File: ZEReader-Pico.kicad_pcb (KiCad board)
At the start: 2 copper layers, 110 x 110 mm, 85 parts, among them J1 Micro_SD_Card_Det2, J2 UART, J3 SWD, J4 USB4105-GF-A, J6 Conn_01x02_Socket, J7 FFC2B28-24-G, Q1 Si1308EDL, Q2 DMG2305UX-7, SW1 SW_Push, SW2 SW_Push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

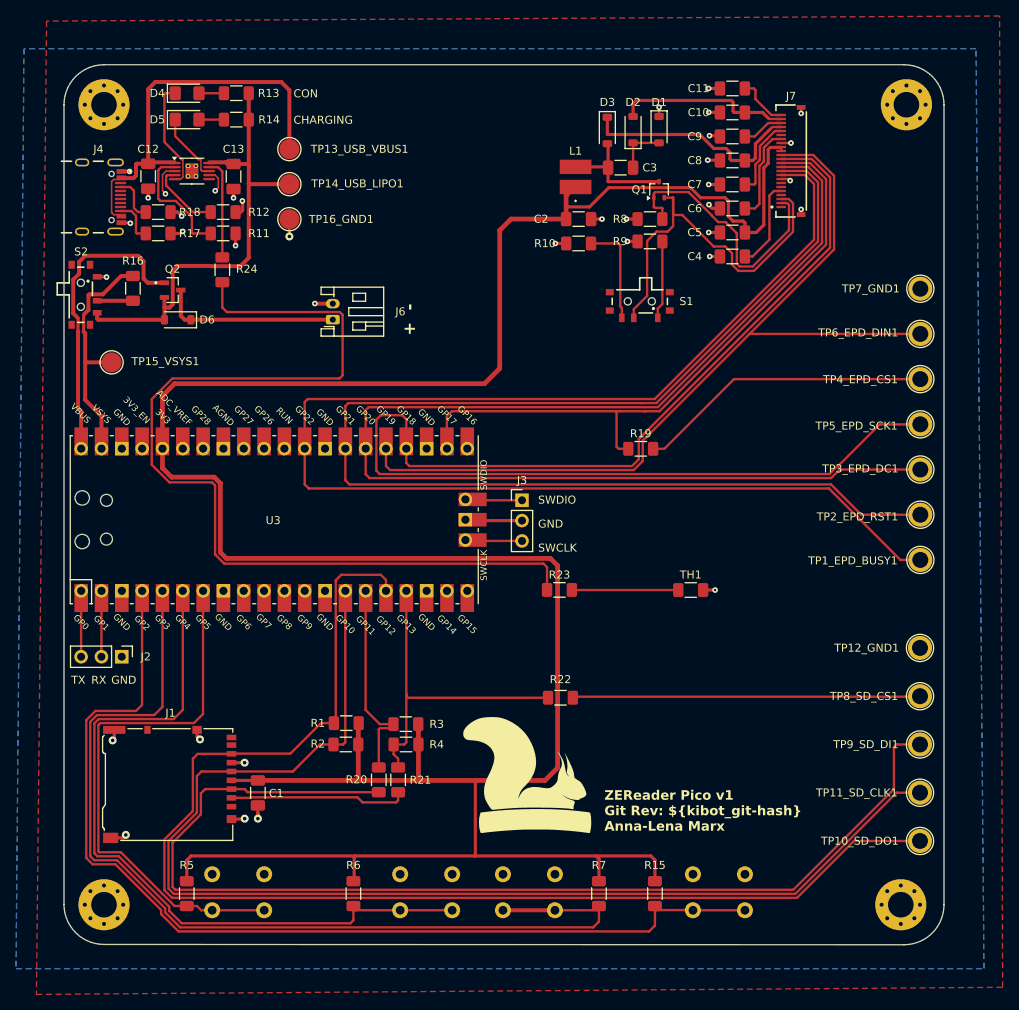
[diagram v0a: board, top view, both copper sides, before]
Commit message: Rerouted two parts
Signed-off-by: Anna-Lena Marx <anna-lena.marx@web.de>
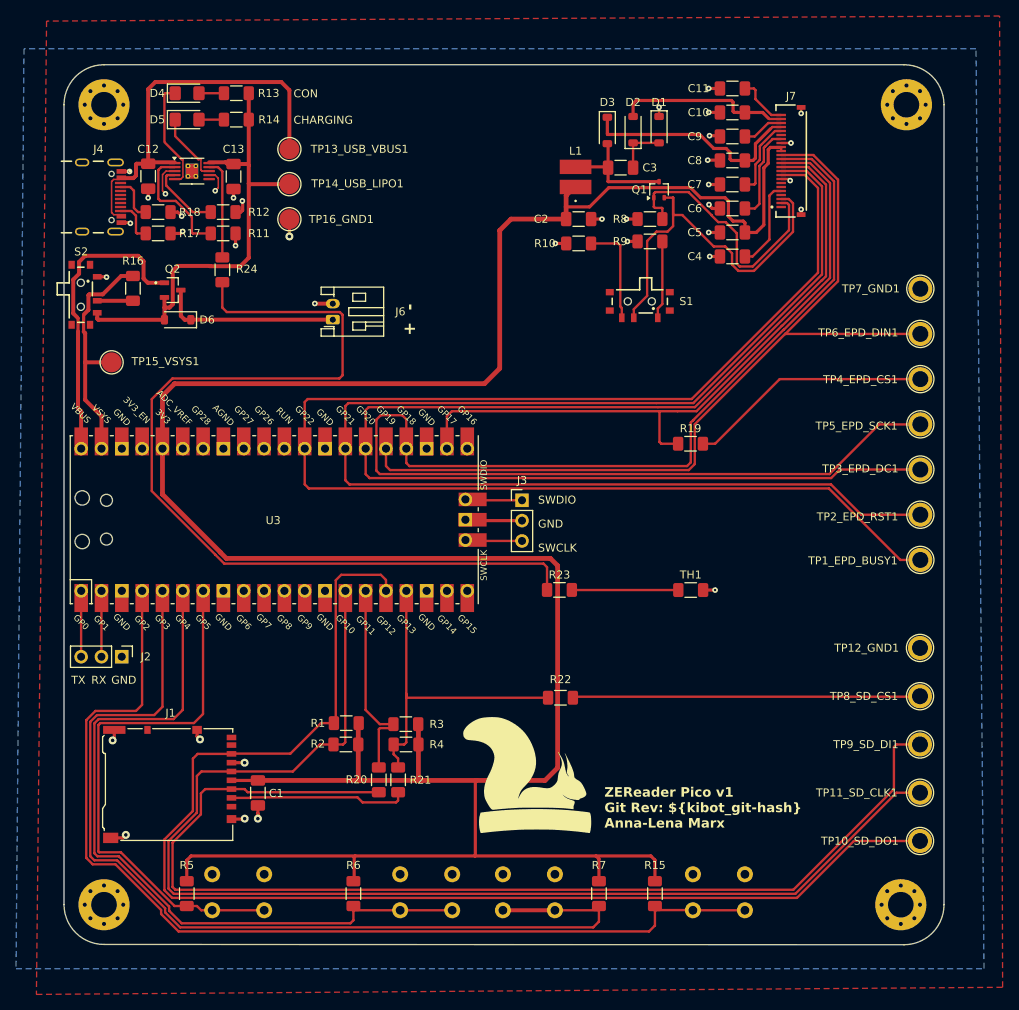
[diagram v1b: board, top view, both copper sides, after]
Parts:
- removed the G*** at (152.0, 131.3)
- removed REF**: KiCad-Logo2_6mm_SilkScreen, Symbol:KiCad-Logo2_6mm_SilkScreen
- added G***: LOGO, prj-footprints:Aisler, B.Cu at (151.6, 132.5)
- moved R19 6.26 mm to (178.4, 87.4)
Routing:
- net Net-(R19-Pad2): track 37.0 -> 30.5 mm
- net EPD_SCK: track 168.5 -> 173.0 mm
- net EPD_CS: track 81.2 -> 84.4 mm
- net EPD_DC: track 157.3 -> 160.4 mm
- net Net-(R23-Pad2): track 122.0 -> 118.9 mm
- net +3.3V: track 347.3 -> 344.2 mm
- net EPD_BUSY: track 174.7 -> 177.9 mm
- net EPD_RST: track 163.3 -> 166.2 mm

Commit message: Optimized track lengths
Signed-off-by: Anna-Lena Marx <anna-lena.marx@web.de>
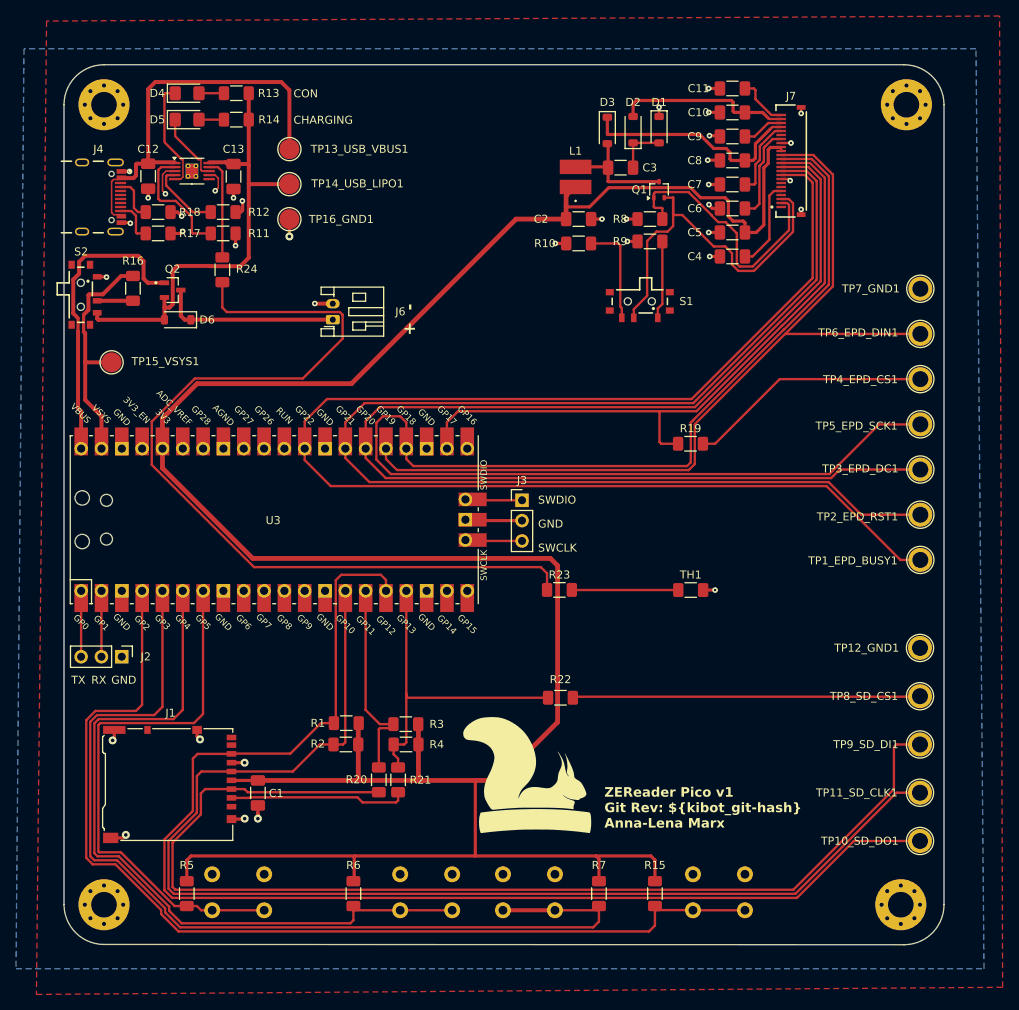
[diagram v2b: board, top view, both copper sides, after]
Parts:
- added REF**: KiCad-Logo2_6mm_SilkScreen, Symbol:KiCad-Logo2_6mm_SilkScreen, B.Cu at (151.3, 124.1)
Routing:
- net +3.3V: track 344.2 -> 327.1 mm
- net Net-(R23-Pad2): track 118.9 -> 112.2 mm
- net EPD_BUSY: track 177.9 -> 174.1 mm
- net EPD_RST: track 166.2 -> 162.8 mm
- net EPD_DC: track 160.4 -> 157.8 mm
- net EPD_SCK: track 173.0 -> 170.8 mm
- net EPD_DIN: track 109.6 -> 108.5 mm
- net EPD_CS: track 84.4 -> 83.4 mm

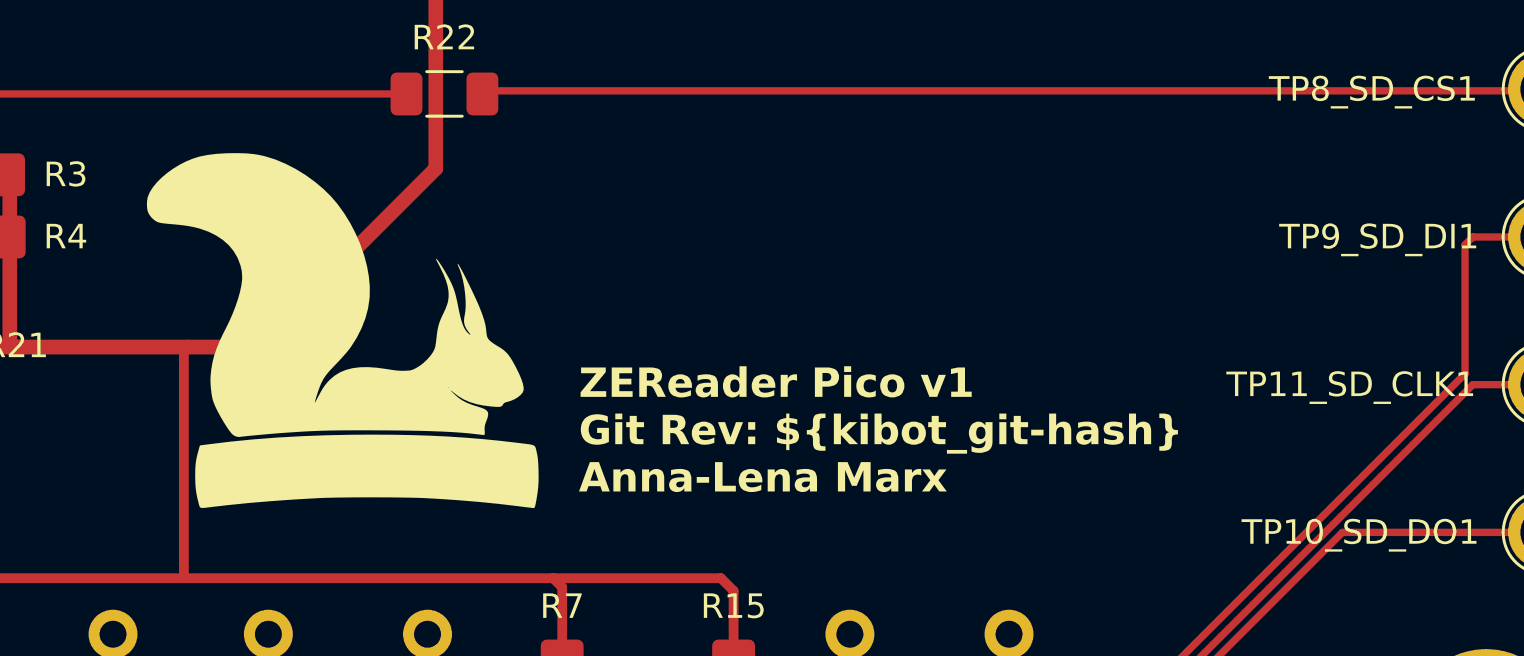
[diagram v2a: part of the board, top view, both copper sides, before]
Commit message: Add kicad_pcb to CI outputs
Signed-off-by: Anna-Lena Marx <anna-lena.marx@web.de>
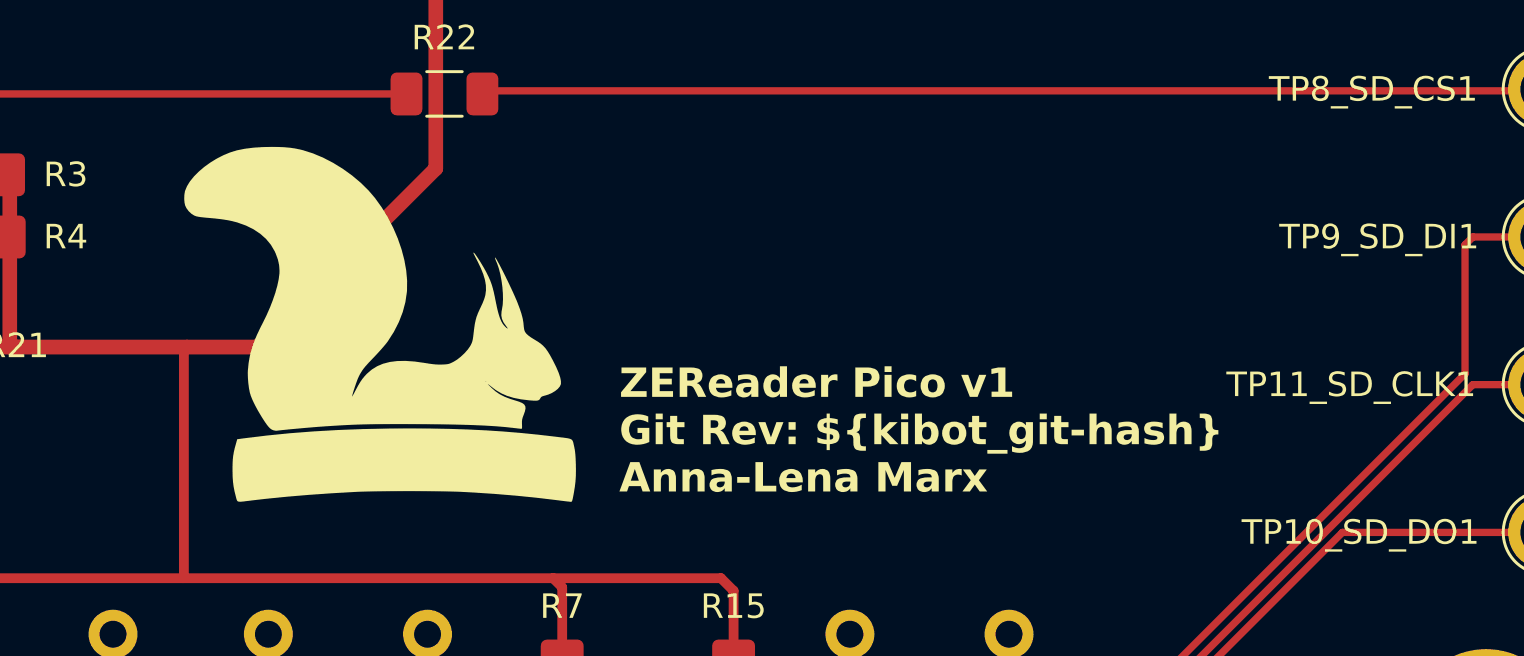
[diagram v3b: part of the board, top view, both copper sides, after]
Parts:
- moved G*** 1.55 mm to (159.5, 128.5)
- moved REF** 0.15 mm to (151.4, 124.0)
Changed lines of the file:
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@@
 	(footprint "prj-footprints:Logo"
 		(layer "F.Cu")
-		(at 157.988 128.778)
+		(at 159.512 128.524)
 		(property "Reference" "G***"
 			(at 0 0 0)
@@
 	(footprint "Symbol:KiCad-Logo2_6mm_SilkScreen"
 		(layer "B.Cu")
-		(at 151.257 124.079 180)
+		(at 151.391487 124.018848 180)
 		(descr "KiCad Logo")
 		(tags "Logo KiCad")
@@
 	)
 	(gr_text "ZEReader Pico v1\nGit Rev: ${kibot_git-hash}\nAnna-Lena Marx"
-		(at 167.64 135.509 0)
+		(at 169.291 135.509 0)
 		(layer "F.SilkS")
 		(effects

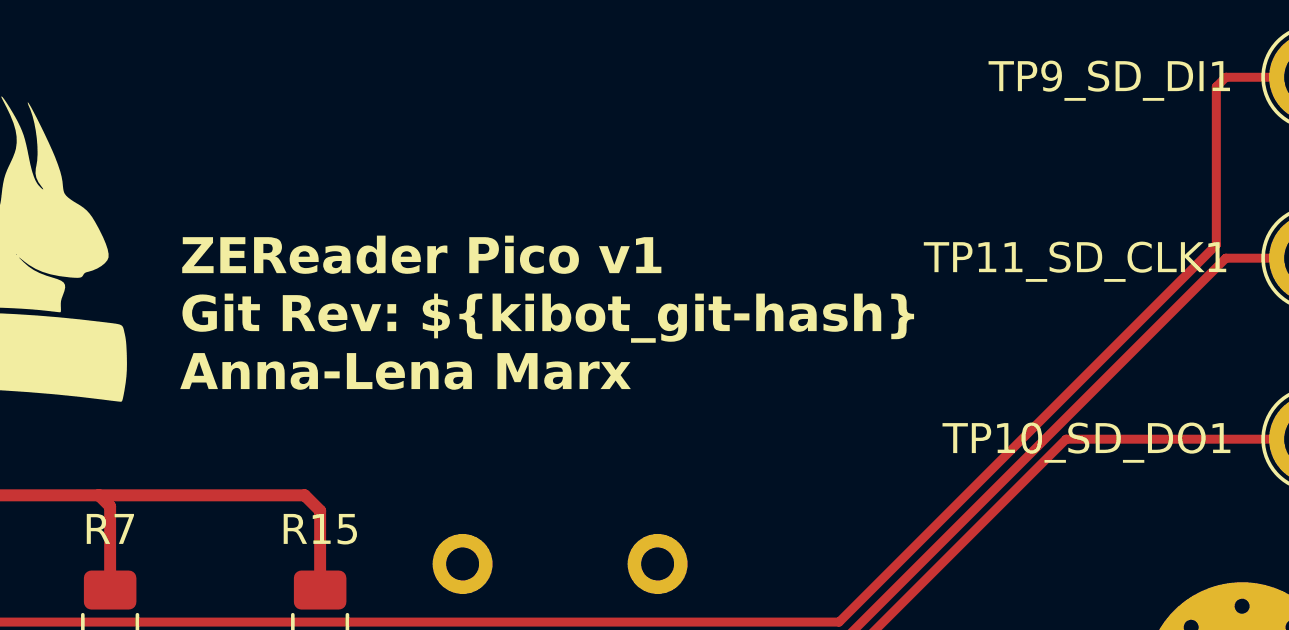
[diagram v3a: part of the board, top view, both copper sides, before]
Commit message: Use sed for variable replacement
Signed-off-by: Anna-Lena Marx <anna-lena.marx@web.de>
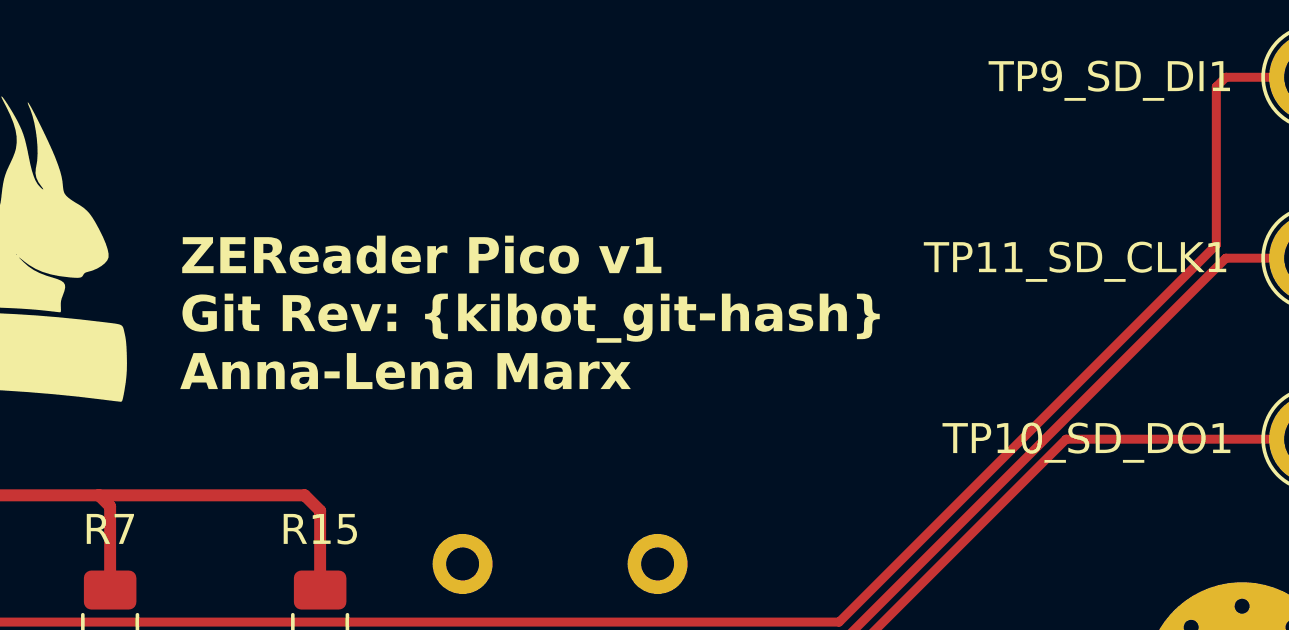
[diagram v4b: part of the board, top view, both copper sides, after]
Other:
- board text added: "ZEReader Pico v1 Git Rev: {kibot_git-hash} Anna-Lena Marx"
- board text removed: "ZEReader Pico v1 Git Rev: ${kibot_git-hash} Anna-Lena Marx"
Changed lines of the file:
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@@
 	(title_block
 		(title "ZEReader-Pico")
-		(date "${kibot_date}")
+		(date "{kibot_date}")
 		(rev "v1")
 		(company "Anna-Lena Marx")
 		(comment 1 "Bachelorthesis")
-		(comment 4 "Git revision: ${kibot_git-hash}")
+		(comment 4 "Git revision: {kibot_git-hash}")
 	)
 	(layers
@@
 		)
 	)
-	(gr_text "ZEReader Pico v1\nGit Rev: ${kibot_git-hash}\nAnna-Lena Marx"
+	(gr_text "ZEReader Pico v1\nGit Rev: {kibot_git-hash}\nAnna-Lena Marx"
 		(at 169.291 135.509 0)
 		(layer "F.SilkS")
